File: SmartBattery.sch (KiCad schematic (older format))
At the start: 52 parts

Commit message: added some more protection connection
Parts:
- added C? (x4): C, symbol Device:C
- added C?: 2.2u, symbol Device:C
- added R? (x3): 100, 0201, symbol Device:R_US
- added R?: 1k, 0201, symbol Device:R_US
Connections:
- net BAT_VN_0 is gone; now on net GNDA: C?.2, C?.2, C?.2, J?.2 (Pin_2), J?.2 (Pin_2), TP?.1, U?.6 (VSS)
- net BAT_VP_0: now also R?.2
- net BAT_VP_1: now also R?.2
- net BAT_VP_2: now also R?.2
- net BAT_VP_3: now also R?.2
- net at U?.1 (PBI): now also C?.1
- net GNDA: now reaches U?.14 (NC/GND)
- net GNDA: now also U?.29 (NC/GND), U?.7 (NC/GND), U?.9 (VSS), C?.2, C?.2
- net at U?.2 (VC4): now also C?.1, R?.1
- net at U?.3 (VC3): now also C?.1, C?.2, R?.1
- net at U?.4 (VC2): now also C?.1, C?.2, R?.1
- net at U?.5 (VC1): now also C?.1, C?.2, R?.1
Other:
- moved on the sheet: C?, R?, U?

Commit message: Almost done with battery protection.
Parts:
- removed U?: BQ2947xx, symbol SmartBattery:BQ2947xx
- removed U?: BQ40Z50, symbol SmartBattery:BQ40Z50
- added C10: 0.1uF, symbol Device:C
- added C11: 0.1u, 0201, symbol Device:C
- added D1, D2, D3, D4, D5: LED, symbol Device:LED
- added Q1, Q2, Q3, Q4: AO4468, Package_TO_SOT_SMD:TDSON-8-1, symbol Device:Q_NMOS_GSD
- added Q5: 2n7002K, symbol Device:Q_NMOS_GSD
- added R13: 10Meg, 0201, symbol Device:R_US
- added R15: DNP, 0201, symbol Device:R_US
- added R16: 0, 0201, symbol Device:R_US
- added R17, R22: 100, 0201, symbol Device:R_US
- added R18, R20, R23: 5.1k, 0201, symbol Device:R_US
- added R19: 0.001, 1206, symbol Device:R_US
- added R21: 100, 201, symbol Device:R_US
- added R24, R25: 10k, 0201, symbol Device:R_US
- added TH1: NCP18WF104F03, 0603, symbol Device:Thermistor_PTC
- added TH2, TH3, TH4, TH5: NXRT15WB473FA1B030, symbol Device:Thermistor_PTC_US
- added TP17, TP18, TP19, TP20: TestPoint, symbol Connector:TestPoint
- gave numbers to parts that had none: 59
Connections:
- net BAT_VP_3: now also C10.2, Q1.2 (S), Q2.2 (S), R13.2, R16.2, TH1.2
- net GNDA: now also R15.2, R17.2, R19.1, TH2.1, TH3.1, TH4.1, TH5.1
- new net: C11.2, R17.1
- new net: C11.1, R21.1
- new net: Q1.1 (G), Q2.1 (G), R13.1, R18.2, TP17.1
- new net: Q1.3 (D), Q2.3 (D), Q3.3 (D), Q4.3 (D), R22.2, TP18.1
- new net: Q3.1 (G), Q4.1 (G), Q5.3 (D), R23.2, TP20.1
- new net: R15.1, R16.1
- new net: C10.1, TH1.1
- new net: R20.2, TP19.1
- new net: Q5.1 (G), R25.2
- new net: D2.1 (K), D3.2 (A), D4.2 (A), D5.1 (K)
- new net: D1.2 (A), D3.1 (K), D5.2 (A)
- new net: D1.1 (K), D2.2 (A), D4.1 (K)
- new net GND: R19.2, R21.2, R25.1
- new net PACK_+: Q3.2 (S), Q4.2 (S), Q5.2 (S), R24.2
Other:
- note added: "LED = 333-2SURC/S530-A3\n5 mm DIP\n"

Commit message: Battery protection sch done. Assigned 99% of footprints. Layout is gonna be rough.
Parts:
- removed C1, C12, C13, C2, C3, C4, C5, C6, C7, C8: C, symbol Device:C
- removed C10: 0.1uF, symbol Device:C
- removed C11: 0.1u, 0201, symbol Device:C
- removed C9: 2.2u, symbol Device:C
- removed D1, D2, D3, D4, D5: LED, symbol Device:LED
- removed F1, F2, F3, F4, F5, F6, F7, F8: Fuse_Small, symbol Device:Fuse_Small
- removed J10, J11, J4, J5, J6, J7, J8, J9: Conn_01x02, symbol Connector_Generic:Conn_01x02
- removed Q1, Q2, Q3, Q4: AO4468, Package_TO_SOT_SMD:TDSON-8-1, symbol Device:Q_NMOS_GSD
- removed Q5: 2n7002K, symbol Device:Q_NMOS_GSD
- removed R1, R2, R3, R4: 1 mOhm, 1206, symbol Device:R_US
- removed R10, R11, R12, R5, R9: 1k, 0201, symbol Device:R_US
- removed R13: 10Meg, 0201, symbol Device:R_US
- removed R14, R17, R22, R6, R7, R8: 100, 0201, symbol Device:R_US
- removed R15: DNP, 0201, symbol Device:R_US
- removed R16: 0, 0201, symbol Device:R_US
- removed R18, R20, R23: 5.1k, 0201, symbol Device:R_US
- removed R19: 0.001, 1206, symbol Device:R_US
- removed R21: 100, 201, symbol Device:R_US
- removed R24, R25: 10k, 0201, symbol Device:R_US
- removed TH1: NCP18WF104F03, 0603, symbol Device:Thermistor_PTC
- removed TH2, TH3, TH4, TH5: NXRT15WB473FA1B030, symbol Device:Thermistor_PTC_US
- removed TP1, TP10, TP11, TP12, TP13, TP14, TP15, TP16, TP17, TP18, TP19, TP2, TP20, TP3, TP4, TP5, TP6, TP7, TP8, TP9: TestPoint, symbol Connector:TestPoint
- J1: footprint (none) -> Connector_USB:USB_C_Receptacle_Amphenol_12401548E4-2A
- J2: value USB_B -> ST-USB-003A; footprint (none) -> Connector_USB:USB3_A_Plug_Wuerth_692112030100_Horizontal
- J3: footprint (none) -> Connector_RJ:RJ45_Amphenol_RJHSE538X
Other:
- note removed: "LED = 333-2SURC/S530-A3\n5 mm DIP\n"

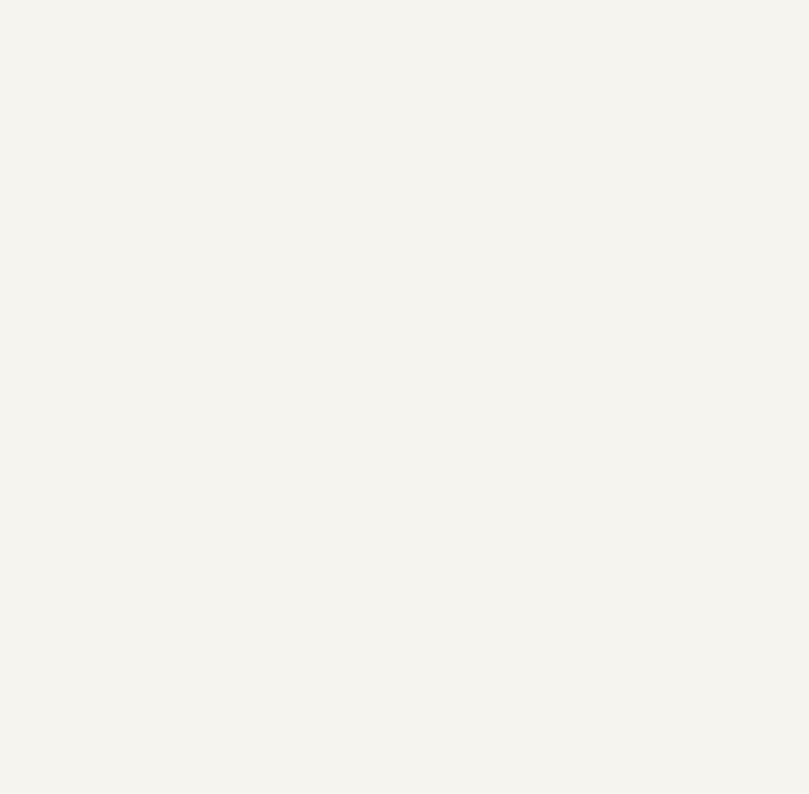
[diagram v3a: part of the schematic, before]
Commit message: Finished battery protection, starting charger page
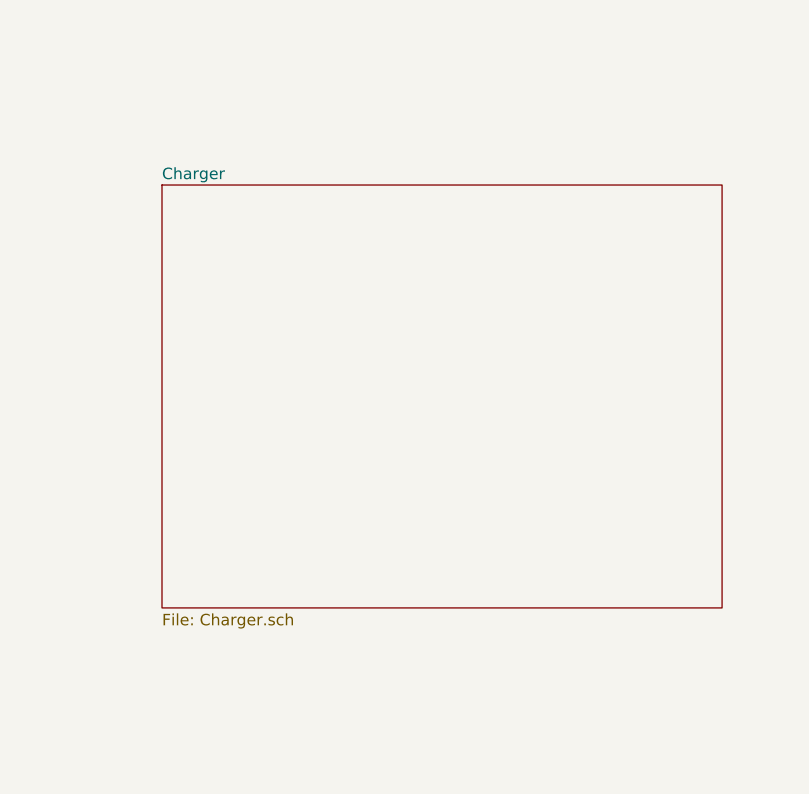
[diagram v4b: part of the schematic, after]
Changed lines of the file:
@@
 $Descr A4 11693 8268
 encoding utf-8
-Sheet 1 2
+Sheet 1 3
 Title ""
 Date ""
@@
 F1 "Battery_Protection.sch" 50
 $EndSheet
+$Sheet
+S 15550 2300 2450 1850
+U 5FD99B08
+F0 "Charger" 50
+F1 "Charger.sch" 50
+$EndSheet
 $EndSCHEMATC

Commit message: Added capacitors, inductors to charger page. Fixed capacitor sizes.
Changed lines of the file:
@@
 $EndComp
 $Sheet
-S 15600 -1300 2700 2300
-U 5FD15753
-F0 "Battery connection and protection" 50
-F1 "Battery_Protection.sch" 50
-$EndSheet
-$Sheet
-S 15550 2300 2450 1850
+S 3000 4750 2450 1850
 U 5FD99B08
 F0 "Charger" 50
 F1 "Charger.sch" 50
 $EndSheet
+$Sheet
+S 2100 2750 1600 950
+U 5FD15753
+F0 "Battery connection and protection" 50
+F1 "Battery_Protection.sch" 50
+F2 "BATT_PACK_P" B R 3700 2900 50
+F3 "BATT_SMB_D" B R 3700 3150 50
+F4 "BATT_SMB_C" B R 3700 3250 50
+F5 "BATT_SHUTDOWN_N" B R 3700 3600 50
+F6 "BATT_INT" B R 3700 3350 50
+$EndSheet
 $EndSCHEMATC

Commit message: Adding lots of changes. Started output Stage
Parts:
- removed J3: RJ45_LED_Shielded, Connector_RJ:RJ45_Amphenol_RJHSE538X, symbol Connector:RJ45_LED_Shielded
- added J3: Barrel_Jack_MountingPin, Connector_BarrelJack:BarrelJack_Horizontal, symbol Connector:Barrel_Jack_MountingPin
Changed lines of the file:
@@
 $Descr A4 11693 8268
 encoding utf-8
-Sheet 1 3
+Sheet 1 5
 Title ""
 Date ""
@@
 	1    0    0    -1
 $EndComp
-$Comp
-L Connector:RJ45_LED_Shielded J3
-U 1 1 5FD1798F
-P 9750 5700
-F 0 "J3" H 9750 6367 50  0000 C CNN
-F 1 "RJ45_LED_Shielded" H 9750 6276 50  0000 C CNN
-F 2 "Connector_RJ:RJ45_Amphenol_RJHSE538X" V 9750 5725 50  0001 C CNN
-F 3 "~" V 9750 5725 50  0001 C CNN
-	1    9750 5700
-	1    0    0    -1
-$EndComp
 $Sheet
-S 3000 4750 2450 1850
+S 4700 2850 1150 900
 U 5FD99B08
 F0 "Charger" 50
 F1 "Charger.sch" 50
+F2 "BATT_PACK_P" B L 4700 2900 50
+F3 "VSYS" B R 5850 2900 50
+F4 "PMON" I R 5850 3700 50
+F5 "IBAT" I R 5850 3600 50
+F6 "IADP" I R 5850 3500 50
+F7 "ACOK" I R 5850 3400 50
+F8 "PROCHOT_N" I R 5850 3300 50
+F9 "CHARGER_SDA" I R 5850 3200 50
+F10 "CHARGER_SCL" I R 5850 3100 50
+F11 "ADAPTER_IN" I L 4700 3600 50
 $EndSheet
 $Sheet
@@
 F6 "BATT_INT" B R 3700 3350 50
 $EndSheet
+Wire Wire Line
+	3700 2900 4700 2900
+$Comp
+L Connector:Barrel_Jack_MountingPin J3
+U 1 1 60145270
+P 3300 4700
+F 0 "J3" H 3357 5017 50  0000 C CNN
+F 1 "Barrel_Jack_MountingPin" H 3357 4926 50  0000 C CNN
+F 2 "Connector_BarrelJack:BarrelJack_Horizontal" H 3350 4660 50  0001 C CNN
+F 3 "~" H 3350 4660 50  0001 C CNN
+	1    3300 4700
+	1    0    0    -1
+$EndComp
+$Sheet
+S 4700 4900 1150 700
+U 60413DD6
+F0 "OutputStage" 50
+F1 "OutputStage.sch" 50
+$EndSheet
+$Sheet
+S 2150 5450 1150 350
+U 6041786F
+F0 "Peripheral_3p3v" 50
+F1 "Peripheral_3p3v.sch" 50
+$EndSheet
 $EndSCHEMATC

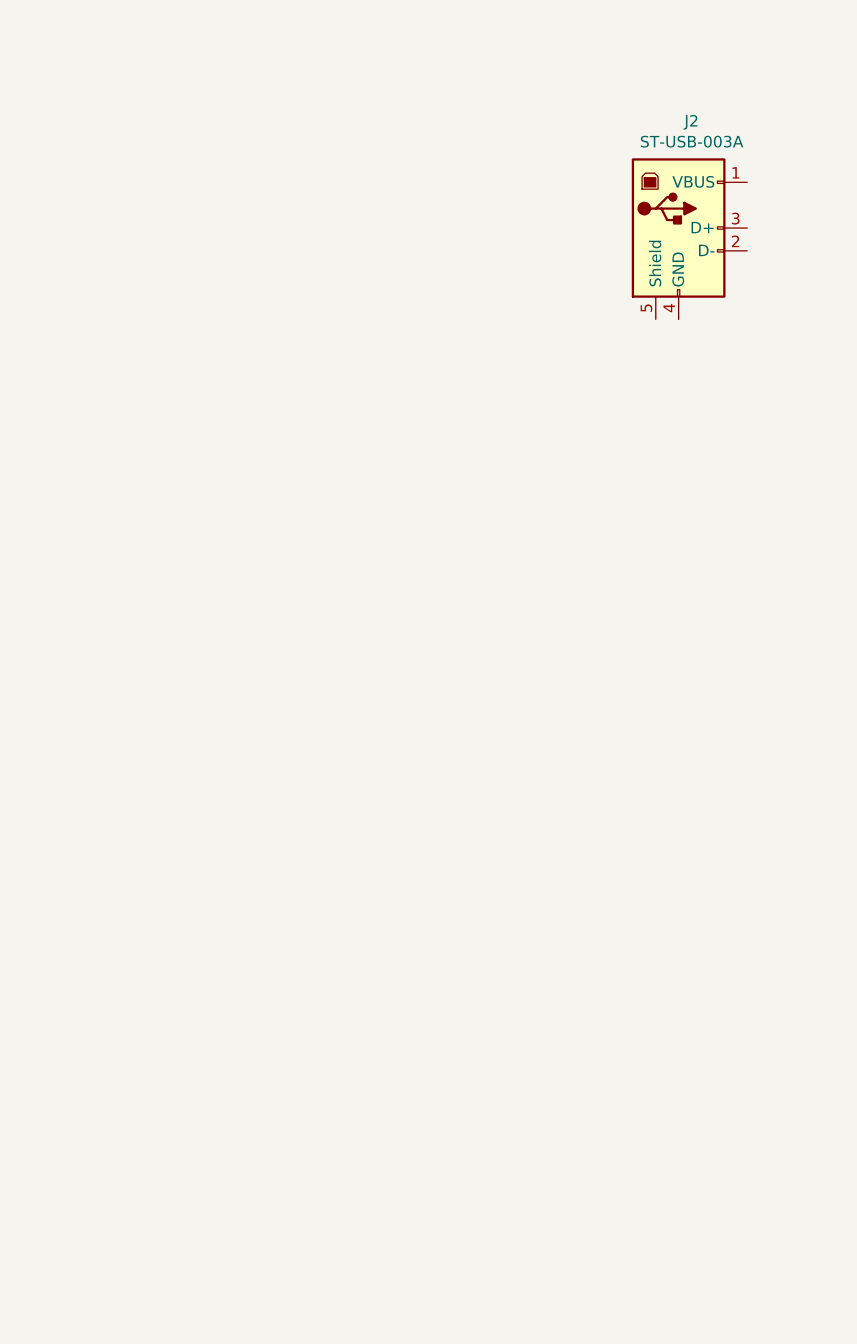
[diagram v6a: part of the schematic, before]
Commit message: Lots of changes for MFG: parts info
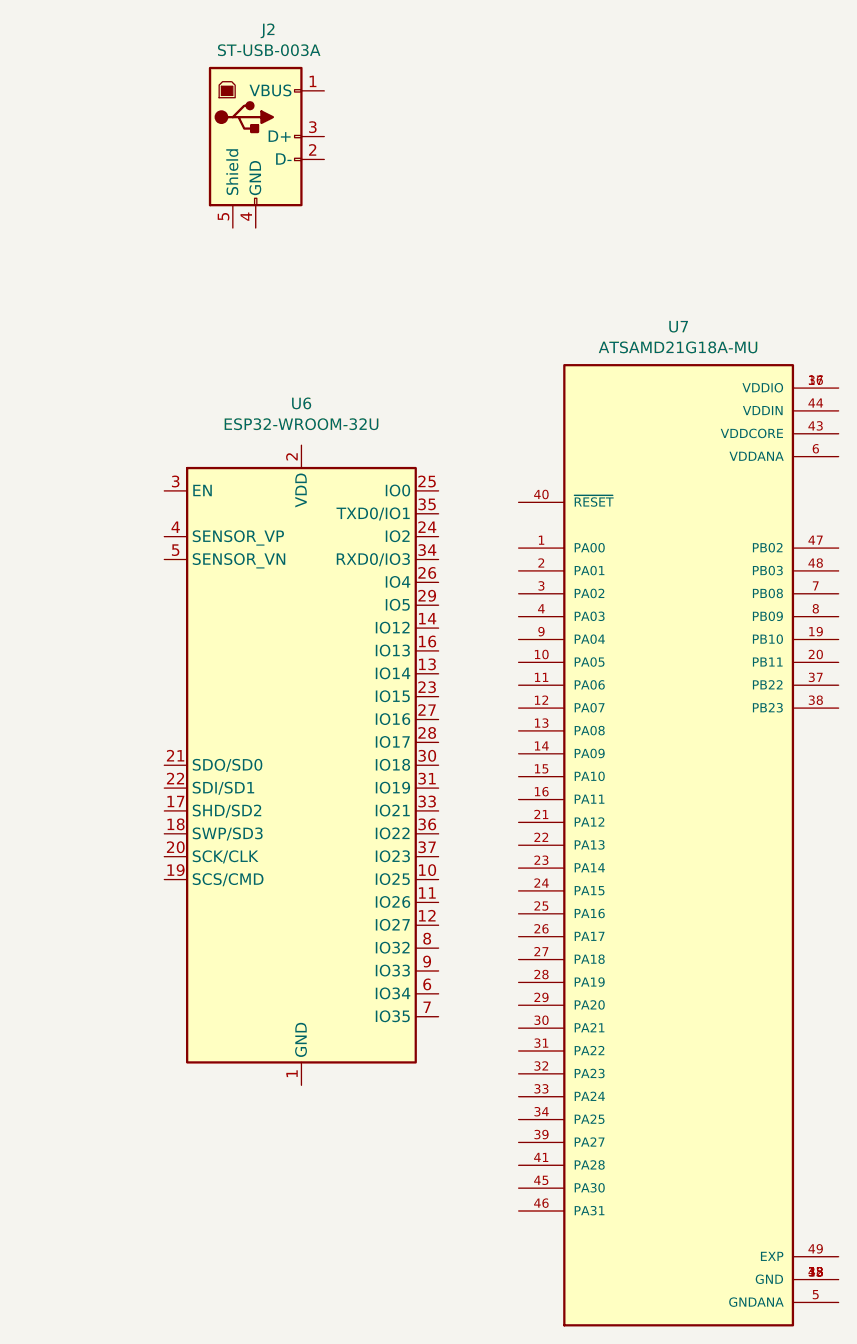
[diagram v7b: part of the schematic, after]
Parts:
- added U6: ESP32-WROOM-32U, RF_Module:ESP32-WROOM-32U, symbol RF_Module:ESP32-WROOM-32U
- added U7: ATSAMD21G18A-MU, SmartBattery:QFN50P700X700X90-49N, symbol SmartBattery:ATSAMD21G18A-MU
- J1: SKU (none) -> TYPE-C-31-M-17
- J2: SKU (none) -> 320010007
- J3: SKU (none) -> 320120003
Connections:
- new net: U6.1 (GND), U6.15 (GND), U6.38 (GND)
- new net: U7.17 (VDDIO), U7.36 (VDDIO)
- new net: U7.18 (GND), U7.35 (GND), U7.42 (GND)
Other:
- moved on the sheet: J2
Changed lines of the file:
@@
 $EndDescr
-$Comp
-L Connector:USB_C_Receptacle_USB2.0 J1
-U 1 1 5FD13F83
-P 1300 1800
-F 0 "J1" H 1407 2667 50  0000 C CNN
-F 1 "USB_C_Receptacle_USB2.0" H 1407 2576 50  0000 C CNN
-F 2 "Connector_USB:USB_C_Receptacle_Amphenol_12401548E4-2A" H 1450 1800 50  0001 C CNN
-F 3 "https://www.usb.org/sites/default/files/documents/usb_type-c.zip" H 1450 1800 50  0001 C CNN
-	1    1300 1800
-	1    0    0    -1
-$EndComp
 $Comp
 L Connector:USB_B J2
 U 1 1 5FD1640D
-P 9750 1650
-F 0 "J2" H 9807 2117 50  0000 C CNN
-F 1 "ST-USB-003A" H 9807 2026 50  0000 C CNN
-F 2 "Connector_USB:USB3_A_Plug_Wuerth_692112030100_Horizontal" H 9900 1600 50  0001 C CNN
-F 3 " ~" H 9900 1600 50  0001 C CNN
-	1    9750 1650
+P 7900 1250
+F 0 "J2" H 7957 1717 50  0000 C CNN
+F 1 "ST-USB-003A" H 7957 1626 50  0000 C CNN
+F 2 "Connector_USB:USB3_A_Plug_Wuerth_692112030100_Horizontal" H 8050 1200 50  0001 C CNN
+F 3 " ~" H 8050 1200 50  0001 C CNN
+F 4 "320010007" H 7900 1250 50  0001 C CNN "SKU"
+	1    7900 1250
 	1    0    0    -1
 $EndComp
@@
 F 2 "Connector_BarrelJack:BarrelJack_Horizontal" H 3350 4660 50  0001 C CNN
 F 3 "~" H 3350 4660 50  0001 C CNN
+F 4 "320120003" H 3300 4700 50  0001 C CNN "SKU"
 	1    3300 4700
 	1    0    0    -1
@@
 F1 "Peripheral_3p3v.sch" 50
 $EndSheet
+$Comp
+L RF_Module:ESP32-WROOM-32U U6
+U 1 1 5FE15F32
+P 8100 4000
+F 0 "U6" H 8100 5581 50  0000 C CNN
+F 1 "ESP32-WROOM-32U" H 8100 5490 50  0000 C CNN
+F 2 "RF_Module:ESP32-WROOM-32U" H 8100 2500 50  0001 C CNN
+F 3 "https://www.espressif.com/sites/default/files/documentation/esp32-wroom-32d_esp32-wroom-32u_datasheet_en.pdf" H 7800 4050 50  0001 C CNN
+F 4 "ESP32-WROOM-32U" H 8100 4000 50  0001 C CNN "SKU"
+	1    8100 4000
+	1    0    0    -1
+$EndComp
+$Comp
+L SmartBattery:ATSAMD21G18A-MU U7
+U 1 1 5FE17BB1
+P 9750 4350
+F 0 "U7" H 9750 6617 50  0000 C CNN
+F 1 "ATSAMD21G18A-MU" H 9750 6526 50  0000 C CNN
+F 2 "SmartBattery:QFN50P700X700X90-49N" H 9750 4350 50  0001 L BNN
+F 3 "" H 9750 4350 50  0001 L BNN
+F 4 "ATSAMD21G18A-MU" H 9750 4350 50  0001 L BNN "MP"
+F 5 "QFN-48 Microchip" H 9750 4350 50  0001 L BNN "PACKAGE"
+F 6 "Good" H 9750 4350 50  0001 L BNN "AVAILABILITY"
+F 7 "IPC-7351B" H 9750 4350 50  0001 L BNN "STANDARD"
+F 8 "2.99 USD" H 9750 4350 50  0001 L BNN "PRICE"
+F 9 "Cortex-M0+, 256KB FLASH, 32KB SRAM, USB, DMA, T&R - 48QFN IND TEMP, GREEN, 1.6-3.6V, 48MHz/ QFN _ZA_" H 9750 4350 50  0001 L BNN "DESCRIPTION"
+F 10 "Microchip" H 9750 4350 50  0001 L BNN "MF"
+F 11 "310010095" H 9750 4350 50  0001 C CNN "SKU"
+	1    9750 4350
+	1    0    0    -1
+$EndComp
+$Comp
+L Connector:USB_C_Receptacle_USB2.0 J1
+U 1 1 5FD13F83
+P 1300 1800
+F 0 "J1" H 1407 2667 50  0000 C CNN
+F 1 "USB_C_Receptacle_USB2.0" H 1407 2576 50  0000 C CNN
+F 2 "Connector_USB:USB_C_Receptacle_Amphenol_12401548E4-2A" H 1450 1800 50  0001 C CNN
+F 3 "https://www.usb.org/sites/default/files/documents/usb_type-c.zip" H 1450 1800 50  0001 C CNN
+F 4 "TYPE-C-31-M-17" H 1300 1800 50  0001 C CNN "SKU"
+	1    1300 1800
+	1    0    0    -1
+$EndComp
 $EndSCHEMATC
